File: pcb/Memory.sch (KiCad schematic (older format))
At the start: 9 parts, among them U5 SDRAM

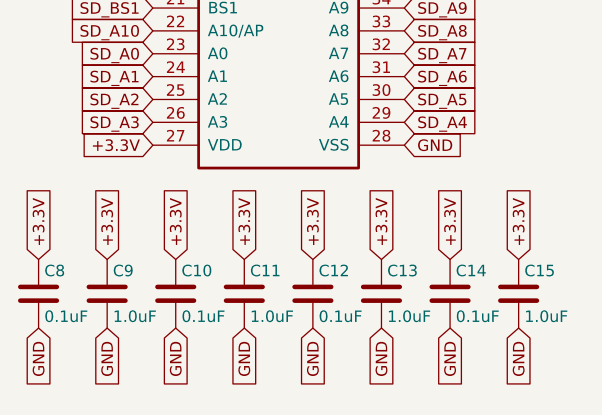
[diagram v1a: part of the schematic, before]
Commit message: Most components placed. FPGA + SDRAM + routing placed off-board.
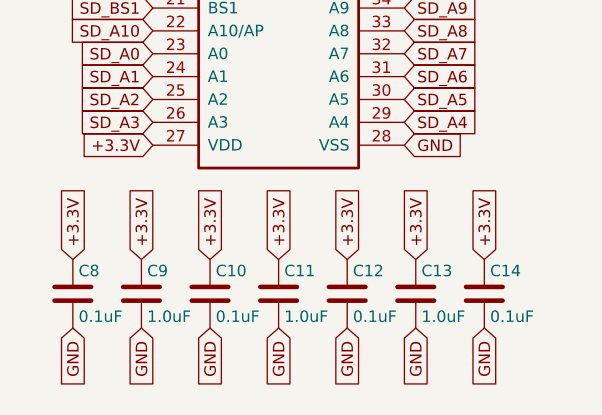
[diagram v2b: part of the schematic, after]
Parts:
- removed C15: 1.0uF, Capacitors_SMD:C_0603_HandSoldering, symbol C
- C10, C11, C12, C13, C14, C8, C9: footprint Capacitors_SMD:C_0603_HandSoldering -> Capacitors_SMD:C_0603
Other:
- moved on the sheet: C10, C11, C12, C13, C14, C8, C9
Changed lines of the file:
@@
 L C C12
 U 1 1 55E9F330
-P 6200 5750
-F 0 "C12" H 6225 5850 50  0000 L CNN
-F 1 "0.1uF" H 6225 5650 50  0000 L CNN
-F 2 "Capacitors_SMD:C_0603_HandSoldering" H 6238 5600 30  0001 C CNN
-F 3 "" H 6200 5750 60  0000 C CNN
-	1    6200 5750
+P 6350 5750
+F 0 "C12" H 6375 5850 50  0000 L CNN
+F 1 "0.1uF" H 6375 5650 50  0000 L CNN
+F 2 "Capacitors_SMD:C_0603" H 6388 5600 30  0001 C CNN
+F 3 "" H 6350 5750 60  0000 C CNN
+	1    6350 5750
 	1    0    0    -1
 $EndComp
@@
 L C C13
 U 1 1 55E9F363
-P 6500 5750
-F 0 "C13" H 6525 5850 50  0000 L CNN
-F 1 "1.0uF" H 6525 5650 50  0000 L CNN
-F 2 "Capacitors_SMD:C_0603_HandSoldering" H 6538 5600 30  0001 C CNN
-F 3 "" H 6500 5750 60  0000 C CNN
-	1    6500 5750
+P 6650 5750
+F 0 "C13" H 6675 5850 50  0000 L CNN
+F 1 "1.0uF" H 6675 5650 50  0000 L CNN
+F 2 "Capacitors_SMD:C_0603" H 6688 5600 30  0001 C CNN
+F 3 "" H 6650 5750 60  0000 C CNN
+	1    6650 5750
 	1    0    0    -1
 $EndComp
-Text GLabel 6200 5600 1    50   Input ~ 0
+Text GLabel 6350 5600 1    50   Input ~ 0
 +3.3V
-Text GLabel 6200 5900 3    50   Input ~ 0
+Text GLabel 6350 5900 3    50   Input ~ 0
 GND
-Text GLabel 6500 5600 1    50   Input ~ 0
+Text GLabel 6650 5600 1    50   Input ~ 0
 +3.3V
-Text GLabel 6500 5900 3    50   Input ~ 0
+Text GLabel 6650 5900 3    50   Input ~ 0
 GND
 $Comp
 L C C14
 U 1 1 55E9F939
-P 6800 5750
-F 0 "C14" H 6825 5850 50  0000 L CNN
-F 1 "0.1uF" H 6825 5650 50  0000 L CNN
-F 2 "Capacitors_SMD:C_0603_HandSoldering" H 6838 5600 30  0001 C CNN
-F 3 "" H 6800 5750 60  0000 C CNN
-	1    6800 5750
+P 6950 5750
+F 0 "C14" H 6975 5850 50  0000 L CNN
+F 1 "0.1uF" H 6975 5650 50  0000 L CNN
+F 2 "Capacitors_SMD:C_0603" H 6988 5600 30  0001 C CNN
+F 3 "" H 6950 5750 60  0000 C CNN
+	1    6950 5750
 	1    0    0    -1
 $EndComp
-$Comp
-L C C15
-U 1 1 55E9F93F
-P 7100 5750
-F 0 "C15" H 7125 5850 50  0000 L CNN
-F 1 "1.0uF" H 7125 5650 50  0000 L CNN
-F 2 "Capacitors_SMD:C_0603_HandSoldering" H 7138 5600 30  0001 C CNN
-F 3 "" H 7100 5750 60  0000 C CNN
-	1    7100 5750
-	1    0    0    -1
-$EndComp
-Text GLabel 6800 5600 1    50   Input ~ 0
-+3.3V
-Text GLabel 6800 5900 3    50   Input ~ 0
-GND
-Text GLabel 7100 5600 1    50   Input ~ 0
+Text GLabel 6950 5600 1    50   Input ~ 0
 +3.3V
-Text GLabel 7100 5900 3    50   Input ~ 0
+Text GLabel 6950 5900 3    50   Input ~ 0
 GND
 $Comp
 L C C8
 U 1 1 55E9FAF7
-P 5000 5750
-F 0 "C8" H 5025 5850 50  0000 L CNN
-F 1 "0.1uF" H 5025 5650 50  0000 L CNN
-F 2 "Capacitors_SMD:C_0603_HandSoldering" H 5038 5600 30  0001 C CNN
-F 3 "" H 5000 5750 60  0000 C CNN
-	1    5000 5750
+P 5150 5750
+F 0 "C8" H 5175 5850 50  0000 L CNN
+F 1 "0.1uF" H 5175 5650 50  0000 L CNN
+F 2 "Capacitors_SMD:C_0603" H 5188 5600 30  0001 C CNN
+F 3 "" H 5150 5750 60  0000 C CNN
+	1    5150 5750
 	1    0    0    -1
 $EndComp
@@
 L C C9
 U 1 1 55E9FAFD
-P 5300 5750
-F 0 "C9" H 5325 5850 50  0000 L CNN
-F 1 "1.0uF" H 5325 5650 50  0000 L CNN
-F 2 "Capacitors_SMD:C_0603_HandSoldering" H 5338 5600 30  0001 C CNN
-F 3 "" H 5300 5750 60  0000 C CNN
-	1    5300 5750
+P 5450 5750
+F 0 "C9" H 5475 5850 50  0000 L CNN
+F 1 "1.0uF" H 5475 5650 50  0000 L CNN
+F 2 "Capacitors_SMD:C_0603" H 5488 5600 30  0001 C CNN
+F 3 "" H 5450 5750 60  0000 C CNN
+	1    5450 5750
 	1    0    0    -1
 $EndComp
-Text GLabel 5000 5600 1    50   Input ~ 0
+Text GLabel 5150 5600 1    50   Input ~ 0
 +3.3V
-Text GLabel 5000 5900 3    50   Input ~ 0
+Text GLabel 5150 5900 3    50   Input ~ 0
 GND
-Text GLabel 5300 5600 1    50   Input ~ 0
+Text GLabel 5450 5600 1    50   Input ~ 0
 +3.3V
-Text GLabel 5300 5900 3    50   Input ~ 0
+Text GLabel 5450 5900 3    50   Input ~ 0
 GND
 $Comp
 L C C10
 U 1 1 55E9FB07
-P 5600 5750
-F 0 "C10" H 5625 5850 50  0000 L CNN
-F 1 "0.1uF" H 5625 5650 50  0000 L CNN
-F 2 "Capacitors_SMD:C_0603_HandSoldering" H 5638 5600 30  0001 C CNN
-F 3 "" H 5600 5750 60  0000 C CNN
-	1    5600 5750
+P 5750 5750
+F 0 "C10" H 5775 5850 50  0000 L CNN
+F 1 "0.1uF" H 5775 5650 50  0000 L CNN
+F 2 "Capacitors_SMD:C_0603" H 5788 5600 30  0001 C CNN
+F 3 "" H 5750 5750 60  0000 C CNN
+	1    5750 5750
 	1    0    0    -1
 $EndComp
@@
 L C C11
 U 1 1 55E9FB0D
-P 5900 5750
-F 0 "C11" H 5925 5850 50  0000 L CNN
-F 1 "1.0uF" H 5925 5650 50  0000 L CNN
-F 2 "Capacitors_SMD:C_0603_HandSoldering" H 5938 5600 30  0001 C CNN
-F 3 "" H 5900 5750 60  0000 C CNN
-	1    5900 5750
+P 6050 5750
+F 0 "C11" H 6075 5850 50  0000 L CNN
+F 1 "1.0uF" H 6075 5650 50  0000 L CNN
+F 2 "Capacitors_SMD:C_0603" H 6088 5600 30  0001 C CNN
+F 3 "" H 6050 5750 60  0000 C CNN
+	1    6050 5750
 	1    0    0    -1
 $EndComp
-Text GLabel 5600 5600 1    50   Input ~ 0
+Text GLabel 5750 5600 1    50   Input ~ 0
 +3.3V
-Text GLabel 5600 5900 3    50   Input ~ 0
+Text GLabel 5750 5900 3    50   Input ~ 0
 GND
-Text GLabel 5900 5600 1    50   Input ~ 0
+Text GLabel 6050 5600 1    50   Input ~ 0
 +3.3V
-Text GLabel 5900 5900 3    50   Input ~ 0
+Text GLabel 6050 5900 3    50   Input ~ 0
 GND
 $Bitmap
@@
 1E 25 49 2A DA F6 C4 5C B7 0C C3 B9 A4 0A 98 09 FC 0D B0 92 CD 57 CD 1F 06 4E 04 26 A7 75 27 49
 52 39 26 13 73 DE C3 6C BE 70 B5 12 F8 16 86 73 8D C3 FF 03 63 F8 EE 2E BE 9A 04 B1 00 00 00 00
-49 45 4E 44 AE 42 60 82 D3
+49 45 4E 44 AE 42 60 82 E5
 EndData
 $EndBitmap
